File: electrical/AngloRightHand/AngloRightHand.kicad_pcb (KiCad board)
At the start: 2 copper layers, 82 x 60 mm, 49 parts, among them J3 TC2030-NL, U1 DRV5053VAQDBZR, U10 DRV5053VAQDBZR, U11 DRV5053VAQDBZR, U12 DRV5053VAQDBZR, U13 DRV5053VAQDBZR, U14 DRV5053VAQDBZR, U15 DRV5053VAQDBZR, U16 STM32L072CBTx, U17 CD74HC4067SM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

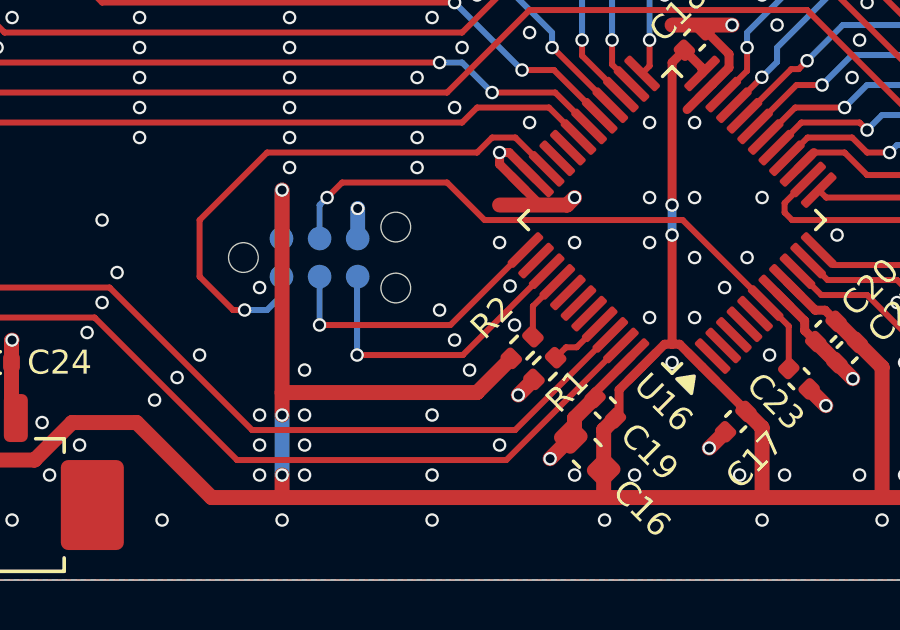
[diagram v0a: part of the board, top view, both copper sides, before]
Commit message: Remove UART from debug connector
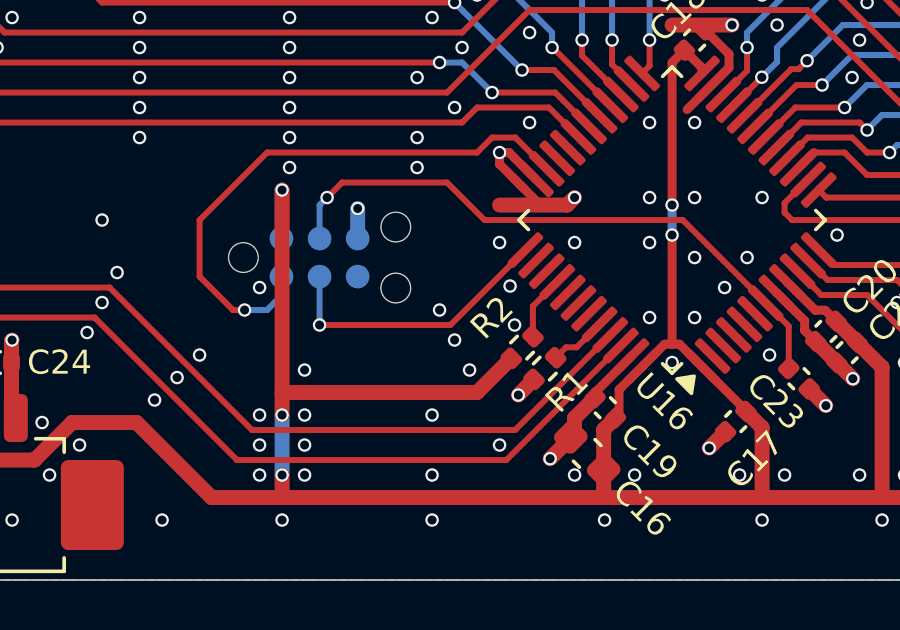
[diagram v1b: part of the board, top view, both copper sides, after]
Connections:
- J3 pad 6: UART_TX -> unconnected-(J3-SWO-Pad6)
- U16 pad 39: UART_TX -> unconnected-(U16-PB3-Pad39)
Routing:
- net UART_TX: track 10.1 -> 0.00 mm, vias 1 -> 0
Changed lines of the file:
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@@
 	(net 9 "SWCLK")
 	(net 10 "SWDIO")
-	(net 11 "UART_TX")
+	(net 11 "unconnected-(J3-SWO-Pad6)")
 	(net 12 "BUTTON_EN_3a")
 	(net 13 "NRST")
@@
 	(net 59 "unconnected-(U16-PA12-Pad33)")
 	(net 60 "Net-(U16-PA1)")
+	(net 61 "unconnected-(U16-PB3-Pad39)")
 	(footprint "Capacitor_SMD:C_0402_1005Metric"
 		(layer "F.Cu")
@@
 			(layers "F.Cu" "F.Mask" "F.Paste")
 			(roundrect_rratio 0.25)
-			(net 11 "UART_TX")
+			(net 61 "unconnected-(U16-PB3-Pad39)")
 			(pinfunction "PB3")
-			(pintype "bidirectional")
+			(pintype "bidirectional+no_connect")
 		)
 		(pad "40" smd roundrect
@@
 			(size 0.7874 0.7874)
 			(layers "B.Cu" "B.Mask")
-			(net 11 "UART_TX")
+			(net 11 "unconnected-(J3-SWO-Pad6)")
 			(pinfunction "SWO")
-			(pintype "input")
+			(pintype "input+no_connect")
 		)
 		(zone
@@
 	)
 	(segment
-		(start 78.5 155.5)
-		(end 82.025127 155.5)
-		(width 0.2)
-		(layer "F.Cu")
-		(net 11)
-	)
-	(segment
-		(start 82.025127 155.5)
-		(end 84.819232 152.705895)
-		(width 0.2)
-		(layer "F.Cu")
-		(net 11)
-	)
-	(via
-		(at 78.5 155.5)
-		(size 0.45)
-		(drill 0.3)
-		(layers "F.Cu" "B.Cu")
-		(net 11)
-	)
-	(segment
-		(start 78.5 155.5)
-		(end 78.5 152.905)
-		(width 0.2)
-		(layer "B.Cu")
-		(net 11)
-	)
-	(segment
-		(start 78.5 152.905)
-		(end 78.52 152.885)
-		(width 0.2)
-		(layer "B.Cu")
-		(net 11)
-	)
-	(segment

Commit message: Use REVISION var to fill silkscreen
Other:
- board text added: "MIDI Anglo Right Hand - Rev ${REVISION}"
- board text removed: "MIDI Anglo Right Hand - Rev 1"
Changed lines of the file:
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@@
 		(layer "Edge.Cuts")
 	)
-	(gr_text "MIDI Anglo Right Hand - Rev 1"
+	(gr_text "MIDI Anglo Right Hand - Rev ${REVISION}"
 		(at 80 106 0)
 		(layer "B.SilkS")

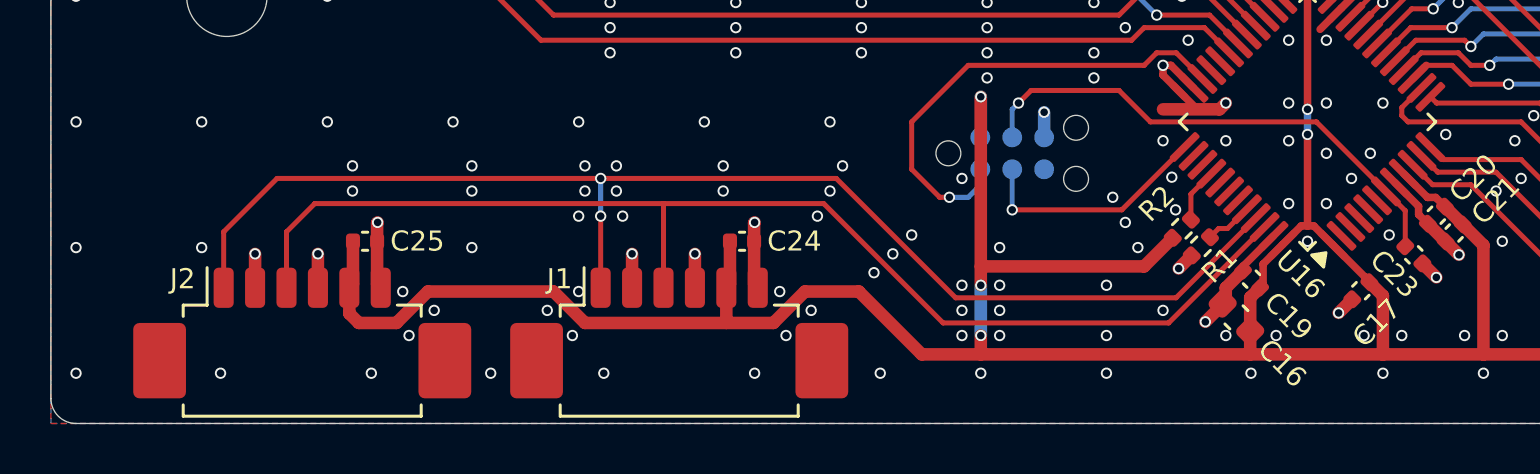
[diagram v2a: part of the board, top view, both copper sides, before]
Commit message: Replace PicoBlade connectors with SKEDD
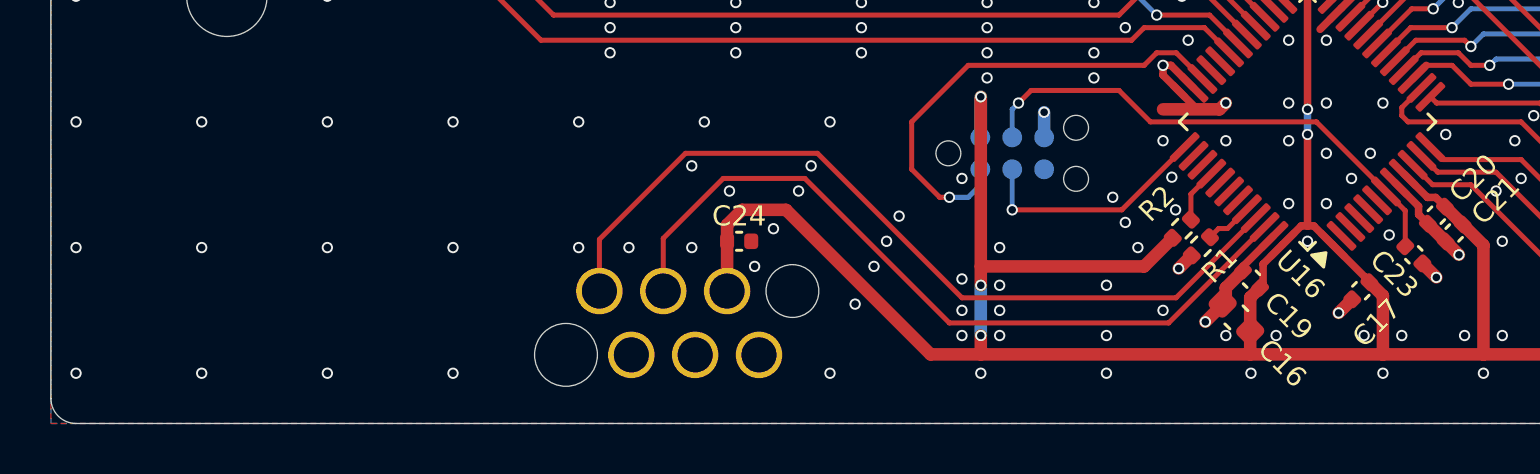
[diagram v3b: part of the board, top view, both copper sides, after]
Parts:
- removed C25: 100nF, Capacitor_SMD:C_0402_1005Metric
- removed J2: ~, Connector_Molex:Molex_PicoBlade_53261-0671_1x06-1MP_P1.25mm_Horizontal
- J1: value ~ -> I2C; footprint Connector_Molex:Molex_PicoBlade_53261-0671_1x06-1MP_P1.25mm_Horizontal -> MidiConcertina:Wuerth_WR-WST_490107670612_2x03_P2.54mm_SKEDD; moved to B.Cu
- moved J1 1.00 mm to (64.0, 159.0), turned to -90 degrees
- moved C24 0.11 mm to (66.4, 155.8)
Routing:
- net +3.3V: track 141.0 -> 122.2 mm
- net I2C_SCL: track 51.8 -> 33.3 mm, vias 2 -> 0
- net I2C_SDA: track 48.5 -> 31.0 mm
- net GND: track 103.7 -> 93.0 mm, vias 517 -> 496

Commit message: Relabel components
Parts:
- renumbered J3 to J2
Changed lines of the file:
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@@
 	(net 9 "SWCLK")
 	(net 10 "SWDIO")
-	(net 11 "unconnected-(J3-SWO-Pad6)")
+	(net 11 "unconnected-(J2-SWO-Pad6)")
 	(net 12 "BUTTON_EN_3a")
 	(net 13 "NRST")
@@
 		(descr "Tag-Connect programming header; http://www.tag-connect.com/Materials/TC2030-IDC-NL.pdf")
 		(tags "tag connect programming header pogo pins")
-		(property "Reference" "J3"
+		(property "Reference" "J2"
 			(at -3.4 0 0)
 			(layer "B.SilkS")
@@
 			(size 0.7874 0.7874)
 			(layers "B.Cu" "B.Mask")
-			(net 11 "unconnected-(J3-SWO-Pad6)")
+			(net 11 "unconnected-(J2-SWO-Pad6)")
 			(pinfunction "SWO")
 			(pintype "input+no_connect")
